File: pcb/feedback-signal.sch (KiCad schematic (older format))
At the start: 13 parts, among them U2 LM321

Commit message: Version 2 PCB design (WIP)
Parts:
- RV1: footprint local:Citec_CB10LV103M -> Local:Citec_CB10LV103M
- renumbered C9 to C7, R28 to R10, R29 to R31, R30 to R32, R26 to R8, R27 to R9, TP46 to TP10, TP47 to TP11, TP48 to TP12, TP49 to TP13, TP45 to TP9
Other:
- moved on the sheet: C7
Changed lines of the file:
@@
 LIBS:valves
 LIBS:symbols
-LIBS:tape-punch-controller-cache
 EELAYER 25 0
 EELAYER END
@@
 F 0 "RV1" V 4875 4600 50  0000 C CNN
 F 1 "10k" V 4950 4600 50  0000 C CNN
-F 2 "local:Citec_CB10LV103M" H 5050 4600 50  0001 C CNN
+F 2 "Local:Citec_CB10LV103M" H 5050 4600 50  0001 C CNN
 F 3 "" H 5050 4600 50  0001 C CNN
 	1    5050 4600
@@
 $EndComp
 $Comp
-L R R28
+L R R10
 U 1 1 5A3C040F
 P 5050 5000
-F 0 "R28" V 5130 5000 50  0000 C CNN
+F 0 "R10" V 5130 5000 50  0000 C CNN
 F 1 "10k" V 5050 5000 50  0000 C CNN
 F 2 "Resistors_SMD:R_0805_HandSoldering" V 4980 5000 50  0001 C CNN
@@
 $EndComp
 $Comp
-L R R26
+L R R8
 U 1 1 5A3C04B2
 P 4200 3250
-F 0 "R26" V 4280 3250 50  0000 C CNN
+F 0 "R8" V 4280 3250 50  0000 C CNN
 F 1 "1k" V 4200 3250 50  0000 C CNN
 F 2 "Resistors_SMD:R_0805_HandSoldering" V 4130 3250 50  0001 C CNN
@@
 $EndComp
 $Comp
-L R R27
+L R R9
 U 1 1 5A3C0507
 P 4200 3650
-F 0 "R27" V 4280 3650 50  0000 C CNN
+F 0 "R9" V 4280 3650 50  0000 C CNN
 F 1 "1k" V 4200 3650 50  0000 C CNN
 F 2 "Resistors_SMD:R_0805_HandSoldering" V 4130 3650 50  0001 C CNN
@@
 $EndComp
 $Comp
-L R R29
+L R R31
 U 1 1 5A3C0552
 P 6850 3800
-F 0 "R29" V 6930 3800 50  0000 C CNN
+F 0 "R31" V 6930 3800 50  0000 C CNN
 F 1 "68k" V 6850 3800 50  0000 C CNN
 F 2 "Resistors_SMD:R_0805_HandSoldering" V 6780 3800 50  0001 C CNN
@@
 $EndComp
 $Comp
-L R R30
+L R R32
 U 1 1 5A3C05C5
 P 6850 4200
-F 0 "R30" V 6930 4200 50  0000 C CNN
+F 0 "R32" V 6930 4200 50  0000 C CNN
 F 1 "18k" V 6850 4200 50  0000 C CNN
 F 2 "Resistors_SMD:R_0805_HandSoldering" V 6780 4200 50  0001 C CNN
@@
 $EndComp
 $Comp
-L C C9
+L C C7
 U 1 1 5A3C0612
-P 8650 5150
-F 0 "C9" H 8675 5250 50  0000 L CNN
-F 1 "100n" H 8675 5050 50  0000 L CNN
-F 2 "Capacitors_SMD:C_0805_HandSoldering" H 8688 5000 50  0001 C CNN
-F 3 "" H 8650 5150 50  0001 C CNN
-	1    8650 5150
+P 9200 5450
+F 0 "C7" H 9225 5550 50  0000 L CNN
+F 1 "100n" H 9225 5350 50  0000 L CNN
+F 2 "Capacitors_SMD:C_0805_HandSoldering" H 9238 5300 50  0001 C CNN
+F 3 "" H 9200 5450 50  0001 C CNN
+	1    9200 5450
 	1    0    0    -1
 $EndComp
@@
 Connection ~ 4200 3450
 $Comp
-L +15V #PWR035
+L +15V #PWR037
 U 1 1 5A3C0DAA
 P 4200 3050
-F 0 "#PWR035" H 4200 2900 50  0001 C CNN
+F 0 "#PWR037" H 4200 2900 50  0001 C CNN
 F 1 "+15V" H 4200 3190 50  0000 C CNN
 F 2 "" H 4200 3050 50  0001 C CNN
@@
 $EndComp
 $Comp
-L GND #PWR036
+L GND #PWR038
 U 1 1 5A3C0E60
 P 4200 3850
-F 0 "#PWR036" H 4200 3600 50  0001 C CNN
+F 0 "#PWR038" H 4200 3600 50  0001 C CNN
 F 1 "GND" H 4200 3700 50  0000 C CNN
 F 2 "" H 4200 3850 50  0001 C CNN
@@
 	5000 3450 5600 3450
 $Comp
-L +15V #PWR037
+L +15V #PWR039
 U 1 1 5A3C1520
 P 5800 3200
-F 0 "#PWR037" H 5800 3050 50  0001 C CNN
+F 0 "#PWR039" H 5800 3050 50  0001 C CNN
 F 1 "+15V" H 5800 3340 50  0000 C CNN
 F 2 "" H 5800 3200 50  0001 C CNN
@@
 $EndComp
 $Comp
-L GND #PWR038
+L GND #PWR040
 U 1 1 5A3C1544
 P 5800 3900
-F 0 "#PWR038" H 5800 3650 50  0001 C CNN
+F 0 "#PWR040" H 5800 3650 50  0001 C CNN
 F 1 "GND" H 5800 3750 50  0000 C CNN
 F 2 "" H 5800 3900 50  0001 C CNN
@@
 	5050 4750 5050 4850
 $Comp
-L GND #PWR039
+L GND #PWR041
 U 1 1 5A3C19BB
 P 5050 5200
-F 0 "#PWR039" H 5050 4950 50  0001 C CNN
+F 0 "#PWR041" H 5050 4950 50  0001 C CNN
 F 1 "GND" H 5050 5050 50  0000 C CNN
 F 2 "" H 5050 5200 50  0001 C CNN
@@
 $EndComp
 $Comp
-L +15V #PWR040
+L +15V #PWR042
 U 1 1 5A3C19E7
 P 5050 4400
-F 0 "#PWR040" H 5050 4250 50  0001 C CNN
+F 0 "#PWR042" H 5050 4250 50  0001 C CNN
 F 1 "+15V" H 5050 4540 50  0000 C CNN
 F 2 "" H 5050 4400 50  0001 C CNN
@@
 Text Label 5400 4500 1    60   ~ 0
 SYNC_THRESHOLD
-Text Notes 8950 5250 0    60   ~ 0
+Text Notes 9500 5550 0    60   ~ 0
 Op-amp decoupling\ncapacitor. Place next\nto supply pin.
 $Comp
-L +15V #PWR041
+L +15V #PWR043
 U 1 1 5A3C4041
-P 8650 4950
-F 0 "#PWR041" H 8650 4800 50  0001 C CNN
-F 1 "+15V" H 8650 5090 50  0000 C CNN
-F 2 "" H 8650 4950 50  0001 C CNN
-F 3 "" H 8650 4950 50  0001 C CNN
-	1    8650 4950
-	1    0    0    -1
-$EndComp
-$Comp
-L GND #PWR042
+P 9200 5250
+F 0 "#PWR043" H 9200 5100 50  0001 C CNN
+F 1 "+15V" H 9200 5390 50  0000 C CNN
+F 2 "" H 9200 5250 50  0001 C CNN
+F 3 "" H 9200 5250 50  0001 C CNN
+	1    9200 5250
+	1    0    0    -1
+$EndComp
+$Comp
+L GND #PWR044
 U 1 1 5A3C4065
-P 8650 5350
-F 0 "#PWR042" H 8650 5100 50  0001 C CNN
-F 1 "GND" H 8650 5200 50  0000 C CNN
-F 2 "" H 8650 5350 50  0001 C CNN
-F 3 "" H 8650 5350 50  0001 C CNN
-	1    8650 5350
-	1    0    0    -1
-$EndComp
-Wire Wire Line
-	8650 4950 8650 5000
-Wire Wire Line
-	8650 5300 8650 5350
+P 9200 5650
+F 0 "#PWR044" H 9200 5400 50  0001 C CNN
+F 1 "GND" H 9200 5500 50  0000 C CNN
+F 2 "" H 9200 5650 50  0001 C CNN
+F 3 "" H 9200 5650 50  0001 C CNN
+	1    9200 5650
+	1    0    0    -1
+$EndComp
+Wire Wire Line
+	9200 5250 9200 5300
+Wire Wire Line
+	9200 5600 9200 5650
 Text Notes 4350 2550 0    60   ~ 0
 The tape punch feedback\ncoil is connected between\nSYNC_COIL- and SYNC_COIL+.
@@
 	6850 3500 6850 3650
 $Comp
-L GND #PWR043
+L GND #PWR045
 U 1 1 5A3C52DE
 P 6850 4400
-F 0 "#PWR043" H 6850 4150 50  0001 C CNN
+F 0 "#PWR045" H 6850 4150 50  0001 C CNN
 F 1 "GND" H 6850 4250 50  0000 C CNN
 F 2 "" H 6850 4400 50  0001 C CNN
@@
 This voltage divider reduces\nthe 15V output voltage to\nabout 3.1V, suitable for the\nmicrocontroller's input pin.
 $Comp
-L TEST TP45
+L TEST TP9
 U 1 1 5A439B1B
 P 4650 3400
-F 0 "TP45" H 4650 3700 50  0000 C BNN
+F 0 "TP9" H 4650 3700 50  0000 C BNN
 F 1 "TEST" H 4650 3650 50  0000 C CNN
 F 2 "Measurement_Points:Measurement_Point_Round-SMD-Pad_Small" H 4650 3400 50  0001 C CNN
@@
 $EndComp
 $Comp
-L TEST TP46
+L TEST TP10
 U 1 1 5A439C40
 P 5200 3400
-F 0 "TP46" H 5200 3700 50  0000 C BNN
+F 0 "TP10" H 5200 3700 50  0000 C BNN
 F 1 "TEST" H 5200 3650 50  0000 C CNN
 F 2 "Measurement_Points:Measurement_Point_Round-SMD-Pad_Small" H 5200 3400 50  0001 C CNN
@@
 Connection ~ 5200 3450
 $Comp
-L TEST TP47
+L TEST TP11
 U 1 1 5A43A093
 P 5400 4650
-F 0 "TP47" H 5400 4950 50  0000 C BNN
+F 0 "TP11" H 5400 4950 50  0000 C BNN
 F 1 "TEST" H 5400 4900 50  0000 C CNN
 F 2 "Measurement_Points:Measurement_Point_Round-SMD-Pad_Small" H 5400 4650 50  0001 C CNN
@@
 Connection ~ 5400 4600
 $Comp
-L TEST TP48
+L TEST TP12
 U 1 1 5A43A451
 P 6850 3500
-F 0 "TP48" H 6850 3800 50  0000 C BNN
+F 0 "TP12" H 6850 3800 50  0000 C BNN
 F 1 "TEST" H 6850 3750 50  0000 C CNN
 F 2 "Measurement_Points:Measurement_Point_Round-SMD-Pad_Small" H 6850 3500 50  0001 C CNN
@@
 $EndComp
 $Comp
-L TEST TP49
+L TEST TP13
 U 1 1 5A43A494
 P 7150 3950
-F 0 "TP49" H 7150 4250 50  0000 C BNN
+F 0 "TP13" H 7150 4250 50  0000 C BNN
 F 1 "TEST" H 7150 4200 50  0000 C CNN
 F 2 "Measurement_Points:Measurement_Point_Round-SMD-Pad_Small" H 7150 3950 50  0001 C CNN

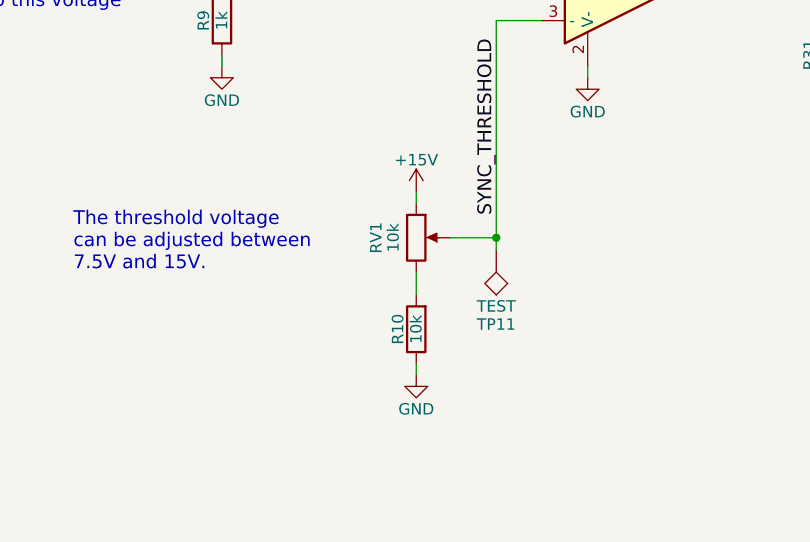
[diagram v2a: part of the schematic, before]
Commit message: pcb: change RV1, RV2 and R10 to be 22k instead of 10k
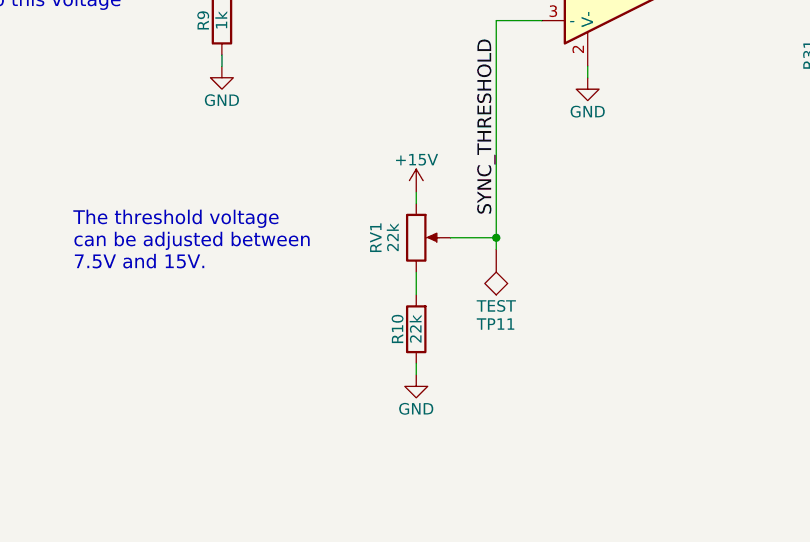
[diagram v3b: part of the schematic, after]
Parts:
- R10, RV1: value 10k -> 22k
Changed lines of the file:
@@
 P 5050 4600
 F 0 "RV1" V 4875 4600 50  0000 C CNN
-F 1 "10k" V 4950 4600 50  0000 C CNN
+F 1 "22k" V 4950 4600 50  0000 C CNN
 F 2 "Local:Citec_CB10LV103M" H 5050 4600 50  0001 C CNN
 F 3 "" H 5050 4600 50  0001 C CNN
@@
 P 5050 5000
 F 0 "R10" V 5130 5000 50  0000 C CNN
-F 1 "10k" V 5050 5000 50  0000 C CNN
+F 1 "22k" V 5050 5000 50  0000 C CNN
 F 2 "Resistors_SMD:R_0805_HandSoldering" V 4980 5000 50  0001 C CNN
 F 3 "" H 5050 5000 50  0001 C CNN
